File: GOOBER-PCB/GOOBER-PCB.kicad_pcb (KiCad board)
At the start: 2 copper layers, 0 parts

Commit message: did some layout
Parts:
- added C1: 10uF, Capacitor_SMD:C_0805_2012Metric_Pad1.18x1.45mm_HandSolder, F.Cu at (51.7, 47.0)
- added C10: 0.1uF, Capacitor_SMD:C_0805_2012Metric_Pad1.18x1.45mm_HandSolder, F.Cu at (50.7, 109.9)
- added C11: 10uF, Capacitor_SMD:C_0805_2012Metric_Pad1.18x1.45mm_HandSolder, F.Cu at (75.8, 53.1)
- added C12: 0.1uF, Capacitor_SMD:C_0805_2012Metric_Pad1.18x1.45mm_HandSolder, F.Cu at (75.8, 51.0)
- added C2: 10uF, Capacitor_SMD:C_0805_2012Metric_Pad1.18x1.45mm_HandSolder, F.Cu at (53.8, 47.0)
- added C3: 0.1uF, Capacitor_SMD:C_0805_2012Metric_Pad1.18x1.45mm_HandSolder, F.Cu at (55.9, 47.0)
- added C4: 0.1uF, Capacitor_SMD:C_0805_2012Metric_Pad1.18x1.45mm_HandSolder, F.Cu at (59.7, 44.0)
- added C5: 22uF, Capacitor_SMD:C_0805_2012Metric_Pad1.18x1.45mm_HandSolder, F.Cu at (65.2, 38.5)
- added C6: 22uF, Capacitor_SMD:C_0805_2012Metric_Pad1.18x1.45mm_HandSolder, F.Cu at (63.1, 38.5)
- added C7: 10uF, Capacitor_SMD:C_0805_2012Metric_Pad1.18x1.45mm_HandSolder, F.Cu at (40.4, 110.1)
- added C8: 0.1uF, Capacitor_SMD:C_0805_2012Metric_Pad1.18x1.45mm_HandSolder, F.Cu at (42.6, 110.1)
- added C9: 10uF, Capacitor_SMD:C_0805_2012Metric_Pad1.18x1.45mm_HandSolder, F.Cu at (48.6, 109.9)
- added D1: LED, LED_SMD:LED_0805_2012Metric, F.Cu at (64.4, 43.5)
- added D2: LED, LED_SMD:LED_0805_2012Metric, F.Cu at (42.4, 19.5)
- added D3: LED, LED_SMD:LED_0805_2012Metric, F.Cu at (40.3, 23.2)
- added D5: CDBW140-G, Diode_SMD:D_SOD-123, F.Cu at (79.9, 47.3)
- added F6: 1A, Fuse:Fuseholder_Blade_Mini_Keystone_3568, F.Cu at (38.1, 39.7)
- added F7: 1A, Fuse:Fuseholder_Blade_Mini_Keystone_3568, F.Cu at (68.3, 47.4)
- added H1: MountingHole, MountingHole:MountingHole_3.2mm_M3_ISO7380, F.Cu at (34.4, 21.6)
- added H2: MountingHole, MountingHole:MountingHole_3.2mm_M3_ISO7380, F.Cu at (78.6, 21.6)
- added H3: MountingHole, MountingHole:MountingHole_3.2mm_M3_ISO7380, F.Cu at (57.9, 110.2)
- added J1: XT30U_F, Connector_AMASS:AMASS_XT30PW-M_1x02_P2.50mm_Horizontal, F.Cu at (53.3, 29.8)
- added J2: Conn_01x22, Connector_PinHeader_2.54mm:PinHeader_1x22_P2.54mm_Vertical, F.Cu at (45.6, 58.1)
- added J3: Conn_01x22, Connector_PinHeader_2.54mm:PinHeader_1x22_P2.54mm_Vertical, F.Cu at (71.0, 58.1)
- added J4: Conn_01x22, Connector_PinHeader_2.54mm:PinHeader_1x22_P2.54mm_Vertical, F.Cu at (37.4, 58.1)
- added J5: Conn_01x22, Connector_PinHeader_2.54mm:PinHeader_1x22_P2.54mm_Vertical, F.Cu at (79.2, 58.1)
- added J6: XT30U_F, Connector_AMASS:AMASS_XT30PW-M_1x02_P2.50mm_Horizontal, F.Cu at (68.6, 29.8)
- added J8: USB C vertical, Connector_USB:USB_C_Receptacle_GCT_USB4115-03-C, F.Cu at (80.6, 37.2)
- added L1: 3.3uH, Inductor_SMD:L_TDK_VLS6045EX_VLS6045AF, F.Cu at (58.7, 39.6)
- added Q3: PJD15P06A_L2_00001, Package_TO_SOT_SMD:TO-252-2, F.Cu at (47.0, 40.9)
- added Q4: AO3419, Package_TO_SOT_SMD:SOT-23_Handsoldering, F.Cu at (76.7, 47.2)
- added R1: 54.9K, Resistor_SMD:R_0805_2012Metric_Pad1.20x1.40mm_HandSolder, F.Cu at (56.9, 51.1)
- added R11: 10K, Resistor_SMD:R_0805_2012Metric_Pad1.20x1.40mm_HandSolder, F.Cu at (59.8, 50.3)
- added R13: 0, Resistor_SMD:R_1210_3225Metric_Pad1.30x2.65mm_HandSolder, F.Cu at (39.6, 45.5)
- added R2: 10K, Resistor_SMD:R_0805_2012Metric_Pad1.20x1.40mm_HandSolder, F.Cu at (54.9, 51.1)
- added R3: 1K, Resistor_SMD:R_0805_2012Metric_Pad1.20x1.40mm_HandSolder, F.Cu at (42.4, 23.2)
- added R4: 1K, Resistor_SMD:R_0805_2012Metric_Pad1.20x1.40mm_HandSolder, F.Cu at (65.3, 46.4)
- added R5: 1K, Resistor_SMD:R_0805_2012Metric_Pad1.20x1.40mm_HandSolder, F.Cu at (40.3, 19.5)
- added R6: 100K, Resistor_SMD:R_0805_2012Metric_Pad1.20x1.40mm_HandSolder, F.Cu at (78.7, 43.4)
- added R7: 5.1K, Resistor_SMD:R_0805_2012Metric_Pad1.20x1.40mm_HandSolder, F.Cu at (78.9, 32.9)
- added R8: 5.1K, Resistor_SMD:R_0805_2012Metric_Pad1.20x1.40mm_HandSolder, F.Cu at (82.4, 41.4)
- added R9: 100, Resistor_SMD:R_0805_2012Metric_Pad1.20x1.40mm_HandSolder, F.Cu at (42.4, 47.0)
- added TP1: TP, TestPoint:TestPoint_Keystone_5000-5004_Miniature, F.Cu at (28.8, 63.1)
- added TP10: TP, TestPoint:TestPoint_Keystone_5000-5004_Miniature, F.Cu at (28.5, 92.8)
- added TP11: TP, TestPoint:TestPoint_Keystone_5000-5004_Miniature, F.Cu at (28.4, 96.1)
- added TP12: TP, TestPoint:TestPoint_Keystone_5000-5004_Miniature, F.Cu at (28.3, 99.4)
- added TP13: TP, TestPoint:TestPoint_Keystone_5000-5004_Miniature, F.Cu at (28.4, 102.7)
- added TP14: TP, TestPoint:TestPoint_Keystone_5000-5004_Miniature, F.Cu at (28.2, 106.0)
- added TP15: TP, TestPoint:TestPoint_Keystone_5000-5004_Miniature, F.Cu at (28.1, 109.3)
- added TP16: TP, TestPoint:TestPoint_Keystone_5000-5004_Miniature, F.Cu at (28.1, 112.6)
- added TP17: TP, TestPoint:TestPoint_Keystone_5000-5004_Miniature, F.Cu at (23.2, 106.4)
- added TP18: TP, TestPoint:TestPoint_Keystone_5000-5004_Miniature, F.Cu at (23.2, 110.8)
- added TP19: TP, TestPoint:TestPoint_Keystone_5000-5004_Miniature, F.Cu at (88.2, 60.9)
- added TP2: TP, TestPoint:TestPoint_Keystone_5000-5004_Miniature, F.Cu at (28.8, 66.4)
- added TP20: TP, TestPoint:TestPoint_Keystone_5000-5004_Miniature, F.Cu at (88.2, 64.2)
- added TP21: TP, TestPoint:TestPoint_Keystone_5000-5004_Miniature, F.Cu at (88.2, 67.5)
- added TP22: TP, TestPoint:TestPoint_Keystone_5000-5004_Miniature, F.Cu at (88.2, 70.8)
- added TP23: TP, TestPoint:TestPoint_Keystone_5000-5004_Miniature, F.Cu at (88.1, 74.1)
- added TP24: TP, TestPoint:TestPoint_Keystone_5000-5004_Miniature, F.Cu at (88.1, 77.4)
- added TP25: TP, TestPoint:TestPoint_Keystone_5000-5004_Miniature, F.Cu at (88.7, 80.7)
- added TP26: TP, TestPoint:TestPoint_Keystone_5000-5004_Miniature, F.Cu at (88.7, 84.0)
- added TP27: TP, TestPoint:TestPoint_Keystone_5000-5004_Miniature, F.Cu at (88.8, 87.3)
- added TP28: TP, TestPoint:TestPoint_Keystone_5000-5004_Miniature, F.Cu at (88.9, 90.6)
- added TP29: TP, TestPoint:TestPoint_Keystone_5000-5004_Miniature, F.Cu at (88.9, 93.9)
- added TP3: TP, TestPoint:TestPoint_Keystone_5000-5004_Miniature, F.Cu at (28.8, 69.7)
- added TP30: TP, TestPoint:TestPoint_Keystone_5000-5004_Miniature, F.Cu at (88.8, 97.2)
- added TP31: TP, TestPoint:TestPoint_Keystone_5000-5004_Miniature, F.Cu at (89.8, 100.5)
- added TP32: TP, TestPoint:TestPoint_Keystone_5000-5004_Miniature, F.Cu at (88.7, 103.8)
- added TP33: TP, TestPoint:TestPoint_Keystone_5000-5004_Miniature, F.Cu at (88.7, 107.1)
- added TP34: TP, TestPoint:TestPoint_Keystone_5000-5004_Miniature, F.Cu at (88.8, 110.4)
- added TP35: TP, TestPoint:TestPoint_Keystone_5000-5004_Miniature, F.Cu at (95.4, 99.0)
- added TP36: TP, TestPoint:TestPoint_Keystone_5000-5004_Miniature, F.Cu at (95.4, 95.7)
- added TP37: TP, TestPoint:TestPoint_Keystone_5000-5004_Miniature, F.Cu at (95.4, 102.3)
- added TP38: TP, TestPoint:TestPoint_Keystone_5000-5004_Miniature, F.Cu at (84.6, 46.7)
- added TP39: TP, TestPoint:TestPoint_Keystone_5000-5004_Miniature, F.Cu at (70.1, 52.9)
- added TP4: TP, TestPoint:TestPoint_Keystone_5000-5004_Miniature, F.Cu at (28.8, 73.0)
- added TP40: TP, TestPoint:TestPoint_Keystone_5000-5004_Miniature, F.Cu at (33.4, 29.6)
- added TP41: TP, TestPoint:TestPoint_Keystone_5000-5004_Miniature, F.Cu at (84.7, 53.7)
- added TP42: TP, TestPoint:TestPoint_Keystone_5000-5004_Miniature, F.Cu at (65.0, 53.0)
- added TP43: TP, TestPoint:TestPoint_Keystone_5000-5004_Miniature, F.Cu at (33.2, 39.3)
- added TP44: TP, TestPoint:TestPoint_Keystone_5000-5004_Miniature, F.Cu at (28.7, 58.2)
- added TP46: TP, TestPoint:TestPoint_Keystone_5000-5004_Miniature, F.Cu at (33.0, 53.0)
- added TP5: TP, TestPoint:TestPoint_Keystone_5000-5004_Miniature, F.Cu at (28.7, 76.3)
- added TP6: TP, TestPoint:TestPoint_Keystone_5000-5004_Miniature, F.Cu at (28.7, 79.6)
- added TP7: TP, TestPoint:TestPoint_Keystone_5000-5004_Miniature, F.Cu at (28.7, 82.9)
- added TP8: TP, TestPoint:TestPoint_Keystone_5000-5004_Miniature, F.Cu at (28.7, 86.2)
- added TP9: TP, TestPoint:TestPoint_Keystone_5000-5004_Miniature, F.Cu at (28.6, 89.5)
- added U1: TPS565208, Package_TO_SOT_SMD:SOT-23-6, F.Cu at (58.6, 47.1)
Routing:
- net USBD_N: track 0.00 -> 11.1 mm, vias 0 -> 2
- net USBD_P: track 0.00 -> 1.88 mm
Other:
- board outline added: 78 x 101 mm
- board text added: "+5VA +5VA RST GPIO4 GPIO5 GPIO6 GPIO7 GPIO15 GPIO16 GPIO17 GPIO18 GPIO8 GPIO3 GPIO46 GPIO9 GPIO10 GPIO11 GPIO12 GPIO13 GPIO14 +5VA GND"
- board text added: "GND U0_TX U0_RX GPIO1 GPIO2 MTMS MTDI MTDO MTCK GPIO38 GPIO37 GPIO36 GPIO35 GPIO0 GPIO45 SPICLK_P SPICLK_N RTC USBD_P USBD_N GND GND"

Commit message: some work on pcb
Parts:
- added C13: 0.1uF, Capacitor_SMD:C_0805_2012Metric_Pad1.18x1.45mm_HandSolder, F.Cu at (111.4, 48.9)
- added H3: MountingHole, MountingHole:MountingHole_3.2mm_M3_ISO7380, F.Cu at (108.6, 110.0)
- added J20: BM04B-SRSS-TB, Connector_JST:JST_SH_BM04B-SRSS-TB_1x04-1MP_P1.00mm_Vertical, F.Cu at (110.3, 94.8)
- added J7: Conn_01x08, Connector_PinHeader_2.54mm:PinHeader_1x08_P2.54mm_Vertical, F.Cu at (94.7, 46.0)
- added J9: Conn_01x08, Connector_PinHeader_2.54mm:PinHeader_1x08_P2.54mm_Vertical, F.Cu at (94.7, 30.8)
- added R12: 10K, Resistor_SMD:R_0805_2012Metric_Pad1.20x1.40mm_HandSolder, F.Cu at (100.8, 33.7)
- added R15: 10K, Resistor_SMD:R_0805_2012Metric_Pad1.20x1.40mm_HandSolder, F.Cu at (103.3, 93.0)
- added R19: 10K, Resistor_SMD:R_0805_2012Metric_Pad1.20x1.40mm_HandSolder, F.Cu at (101.2, 93.0)
- added TP45: TP, TestPoint:TestPoint_Keystone_5000-5004_Miniature, F.Cu at (27.3, 58.2)
- moved H2 30.0 mm to (108.6, 21.6)
- moved TP44 6.29 mm to (27.4, 52.0)
- moved TP27 2.69 mm to (86.1, 87.3)
- moved TP30 2.69 mm to (86.1, 97.2)
- moved TP31 2.69 mm to (87.1, 100.5)
- moved TP34 2.69 mm to (86.1, 110.4)
- moved TP19 2.69 mm to (85.5, 60.9)
- moved TP20 2.69 mm to (85.5, 64.2)
- moved TP21 2.69 mm to (85.5, 67.5)
- moved TP22 2.69 mm to (85.5, 70.8)
- moved TP23 2.69 mm to (85.4, 74.1)
- moved TP24 2.69 mm to (85.4, 77.4)
- moved TP25 2.69 mm to (86.0, 80.7)
- moved TP26 2.69 mm to (86.0, 84.0)
- moved TP28 2.69 mm to (86.2, 90.6)
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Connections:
- net MTCK renamed CLK
- net MTDI renamed MOSI
- net MTDO renamed MISO
- net MTMS renamed CS
- J2 pad 1: unconnected-(J2-Pin_1-Pad1) -> +3V3
- J2 pad 2: unconnected-(J2-Pin_2-Pad2) -> +3V3
- J4 pad 2: +5VA -> +3V3
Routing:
- net GPIO13: track 0.00 -> 37.6 mm
- net GPIO14: track 0.00 -> 35.0 mm
- net GPIO18: track 0.00 -> 27.7 mm
- net SPICLK_N: track 0.00 -> 27.3 mm
- net GPIO16: track 0.00 -> 27.0 mm
- net GPIO5: track 0.00 -> 25.6 mm
- net GPIO12: track 0.00 -> 25.5 mm
- net GPIO11: track 0.00 -> 24.2 mm
- net GPIO10: track 0.00 -> 23.3 mm
- net SPICLK_P: track 0.00 -> 23.2 mm
- net GPIO0: track 0.00 -> 22.5 mm
- net GPIO45: track 0.00 -> 22.2 mm
- net CS: track 0.00 -> 21.3 mm
- net GPIO35: track 0.00 -> 21.2 mm
- net GPIO36: track 0.00 -> 21.0 mm
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- added copper zone on B.Cu, net GND
- added copper zone on F.Cu, net GND
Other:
- board size 78 x 101 mm -> 99 x 99 mm
- board text added: "+5VA +3V3 RST GPIO4 GPIO5 GPIO6 GPIO7 GPIO15 GPIO16 GPIO17 GPIO18 GPIO8 GPIO3 GPIO46 GPIO9 GPIO10 GPIO11 GPIO12 GPIO13 GPIO14 +5VA GND"
- board text removed: "+5VA +5VA RST GPIO4 GPIO5 GPIO6 GPIO7 GPIO15 GPIO16 GPIO17 GPIO18 GPIO8 GPIO3 GPIO46 GPIO9 GPIO10 GPIO11 GPIO12 GPIO13 GPIO14 +5VA GND"

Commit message: first revision of goober pcb
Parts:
- removed the H3 at (108.6, 110.0)
- removed TP36, TP37: TP, TestPoint:TestPoint_Keystone_5000-5004_Miniature
- moved R19 17.4 mm to (104.4, 110.1), turned to 0 degrees
- moved R15 15.1 mm to (104.4, 108.1), turned to 0 degrees
- moved J20 10.8 mm to (103.7, 103.3), turned to 0 degrees
- moved H2 5.00 mm to (103.6, 21.6)
- moved C13 4.39 mm to (107.2, 50.0)
- moved J7 4.39 mm to (90.4, 47.1)
- moved J9 4.39 mm to (90.4, 31.9)
- moved R12 4.39 mm to (96.5, 34.8)
- moved R8 2.81 mm to (85.2, 41.4)
- moved TP41 1.59 mm to (83.2, 53.1)
- moved TP42 0.76 mm to (65.5, 52.4)
- moved TP39 0.46 mm to (70.1, 52.4)
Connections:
- J7 pad 3: GPIO12 -> GPIO38
- J7 pad 4: GPIO13 -> GPIO37
- J7 pad 5: GPIO14 -> GPIO36
- J9 pad 7: GPIO11 -> GPIO35
- J9 pad 8: GPIO10 -> GPIO0
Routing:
- net +3V3: track 13.2 -> 179.1 mm, vias 0 -> 1
- net USBD_P: track 11.0 -> 147.5 mm
- net +5VA: track 12.5 -> 147.1 mm, vias 0 -> 1
- net USBD_N: track 20.2 -> 144.6 mm
- net GPIO0: track 22.5 -> 115.5 mm
- net GPIO8: track 19.9 -> 111.7 mm
- net GPIO35: track 21.2 -> 109.3 mm
- net GPIO9: track 21.0 -> 107.5 mm, vias 0 -> 2
- net CLK: track 19.9 -> 100.0 mm
- net MISO: track 19.5 -> 98.7 mm
- net MOSI: track 18.6 -> 86.3 mm
- net +12V: track 4.78 -> 71.7 mm, vias 0 -> 1
- net GPIO36: track 21.0 -> 81.6 mm, vias 0 -> 1
- net GPIO37: track 20.7 -> 76.0 mm, vias 0 -> 1
- net CS: track 21.3 -> 74.1 mm
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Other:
- board size 99 x 99 mm -> 90.4 x 99 mm
- board text added: "GOOBER PCB V1"

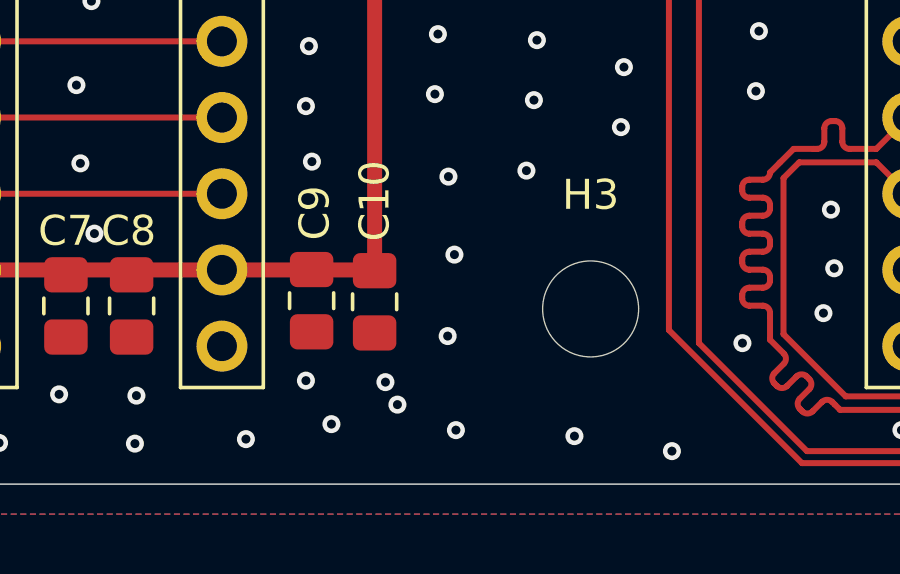
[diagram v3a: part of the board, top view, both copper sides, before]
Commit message: added 47uF cap
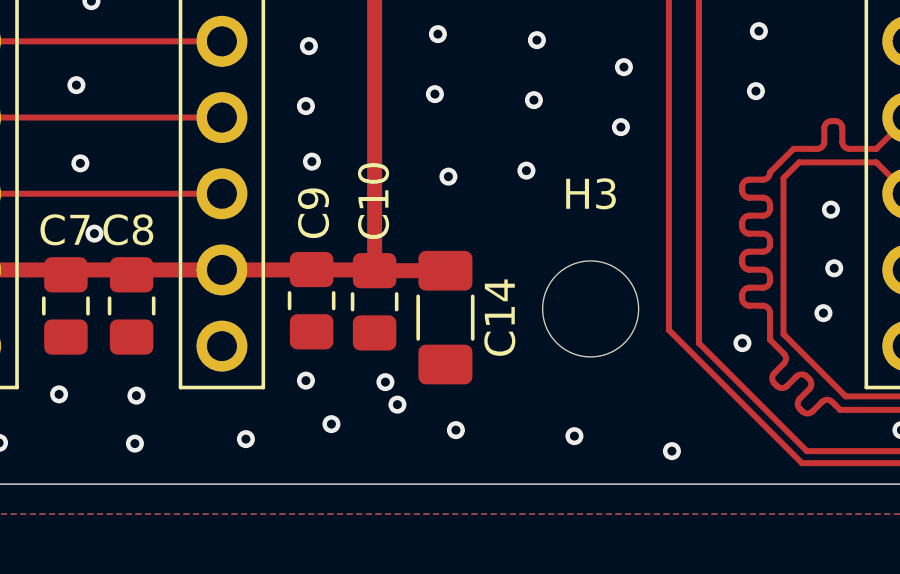
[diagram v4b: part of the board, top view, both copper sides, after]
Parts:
- added C14: 47uF, Capacitor_SMD:C_1206_3216Metric_Pad1.33x1.80mm_HandSolder, F.Cu at (53.0, 110.5)
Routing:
- net +5VA: track 147.1 -> 149.5 mm
- net GND: vias 476 -> 474
